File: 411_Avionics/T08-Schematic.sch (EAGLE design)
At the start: 34 parts, among them IC1 BQ24022, J1 USB-MICROB, U2 M25P10-AVMN6TP_TR, U3 LSM9DS0, U5 LTC1998, U6 ATMEGA32U4-AU, X1 8MHz

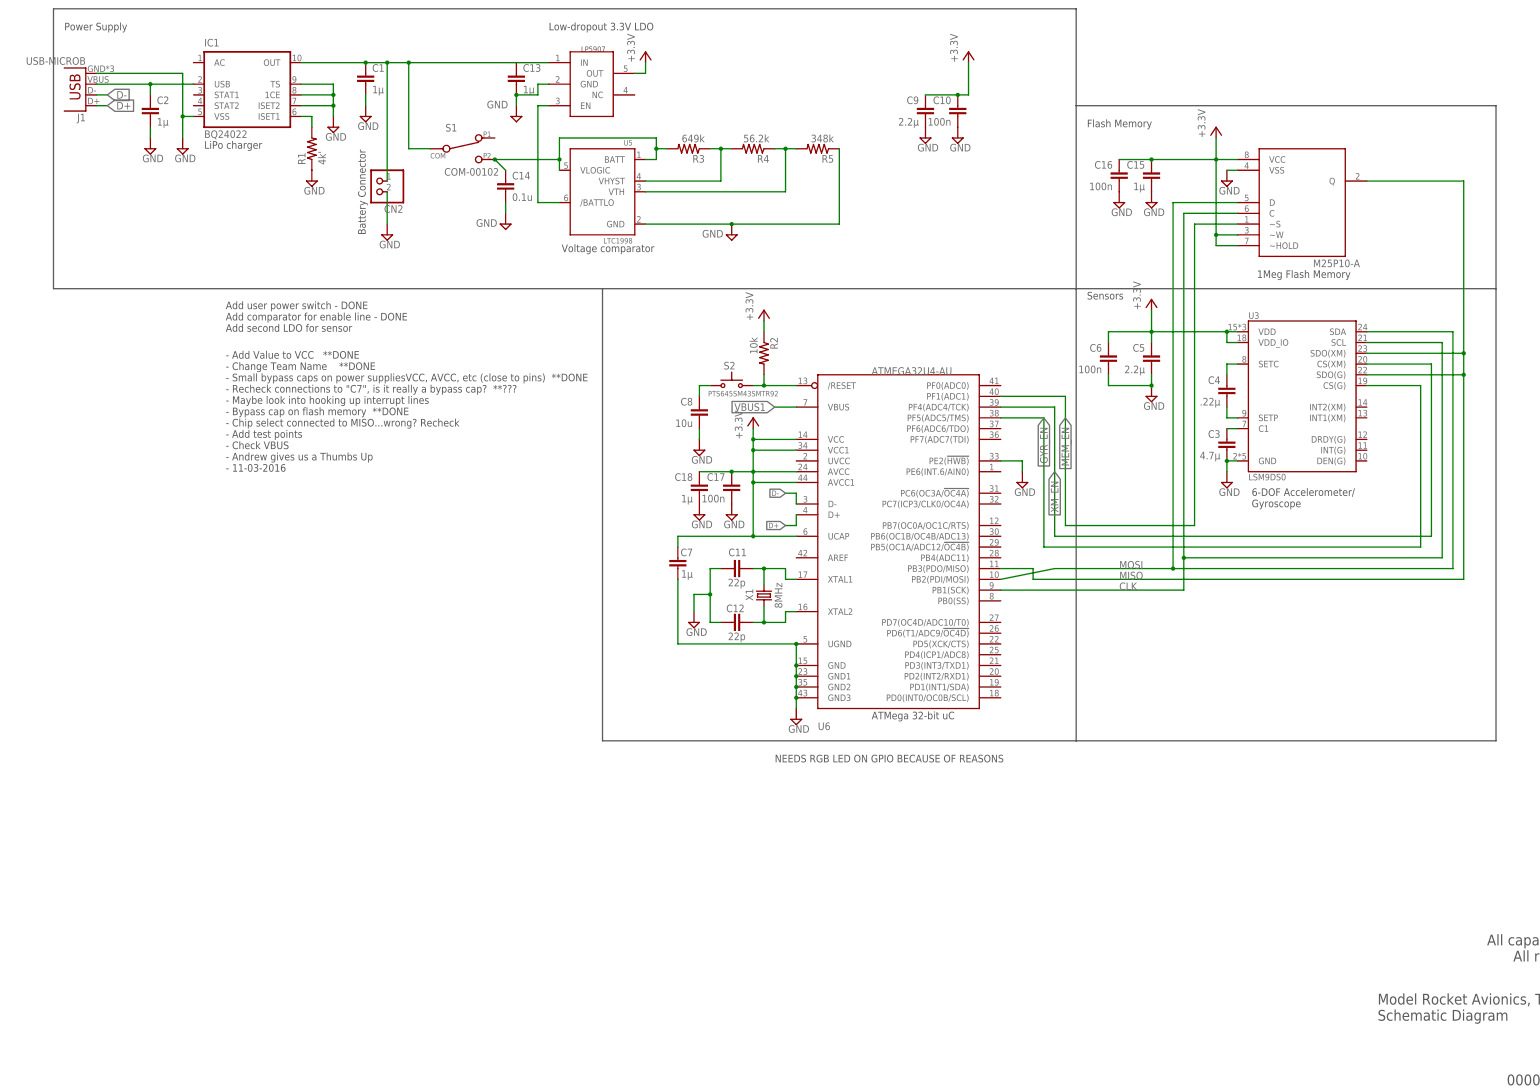
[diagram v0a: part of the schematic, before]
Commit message: Added RGB LED & resolved several ERC errors
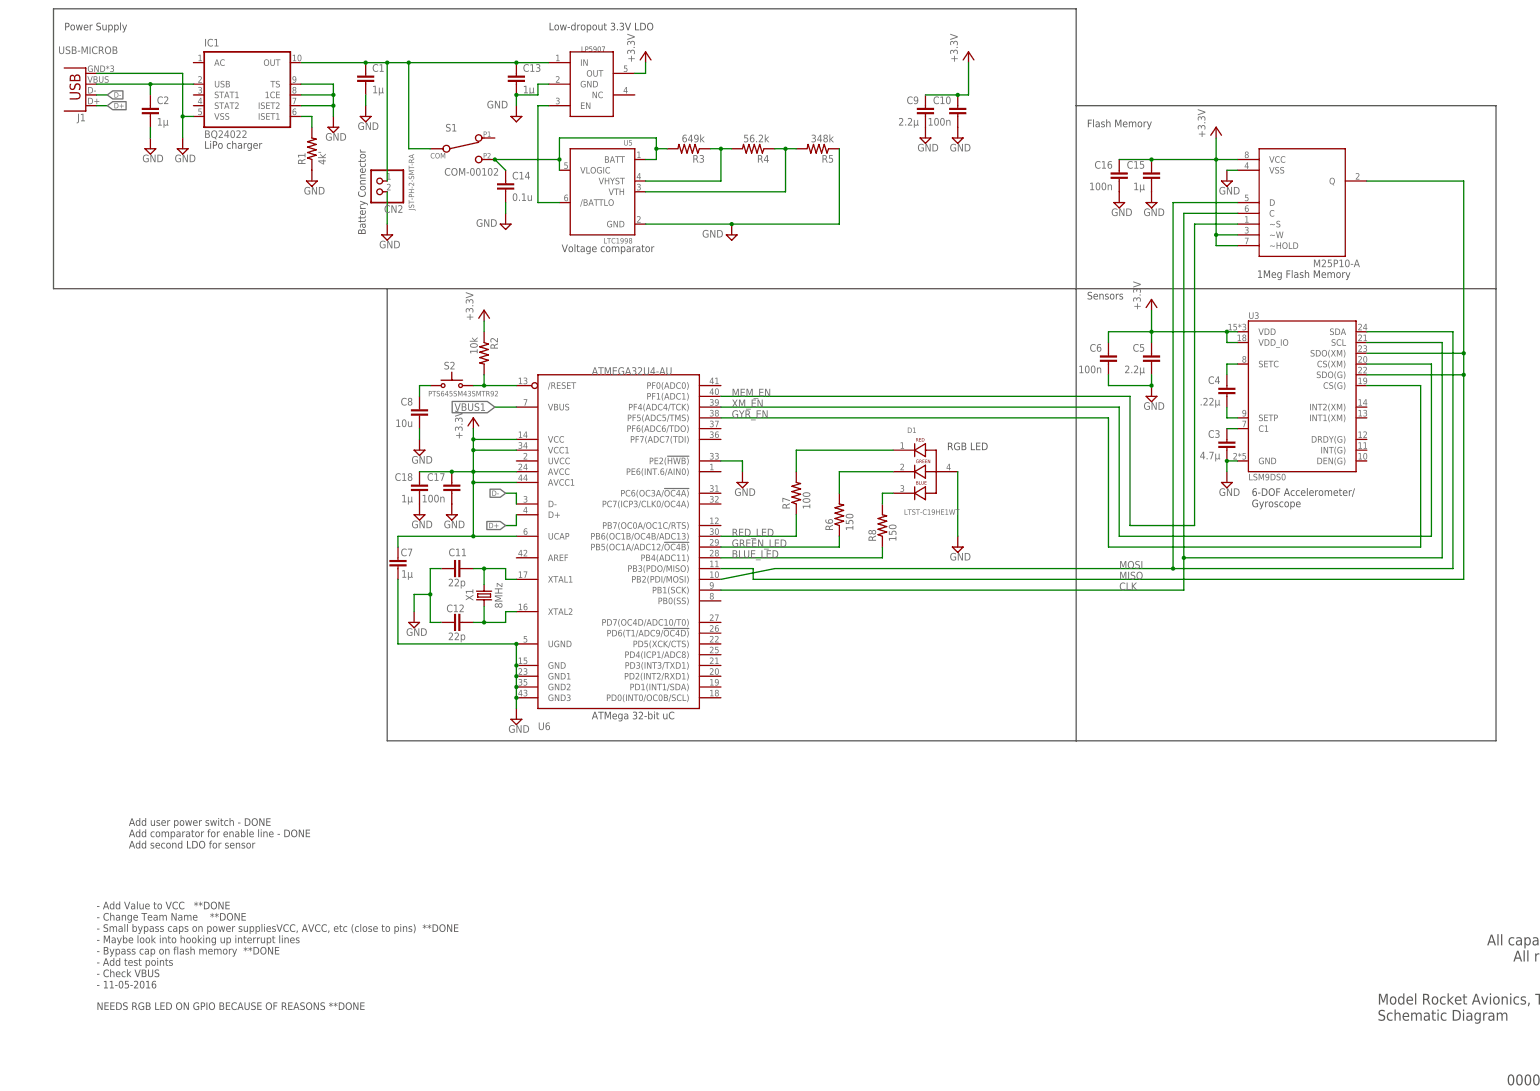
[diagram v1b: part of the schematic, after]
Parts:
- added D1: LTST-C19HE1WT, LTST-C19HE1WT:LTST-C19HE1WT
- added R6, R8: 150, rcl:R-US_R0805
- added R7: 100, rcl:R-US_R0805
- CN2: value (none) -> JST-PH-2-SMT-RA
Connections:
- new net BLUE_LED: R8.1, U6.PB4(ADC11)
- new net GREEN_LED: R6.1, U6.PB5(OC1A/ADC12/!OC4B)
- new net N$8: D1.3, R8.2
- new net RED_LED: R7.1, U6.PB6(OC1B/OC4B/ADC13)
- net GND: now also C13.2, D1.4, U$2.GND
- net N$1: now also D1.1, R7.2; no longer C2.1, IC1G$1.USB, J1.VBUS
- net N$13: now also C13.1
- net N$7: now also D1.2, R6.2; no longer C13.2, U$2.GND
- net VBUS1: now also C2.1, IC1G$1.USB, J1.VBUS
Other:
- note added: "- Add Value to VCC **DONE - Change Team Name **DONE - Small bypass caps on power suppliesVCC, AVCC, etc (close to pins) **DONE - Maybe look into hooking up interrupt lines - Bypass cap on flash memory **DONE - Add test points - Check VBUS - 11-05-2016"
- note added: "NEEDS RGB LED ON GPIO BECAUSE OF REASONS **DONE"
- note added: "RGB LED"
- note removed: "- Add Value to VCC **DONE - Change Team Name **DONE - Small bypass caps on power suppliesVCC, AVCC, etc (close to pins) **DONE - Recheck connections to "C7", is it really a bypass cap? **??? - Maybe look into hooking up interrupt lines - Bypass cap on flash memory **DONE - Chip select connected to MISO...wrong? Recheck - Add test points - Check VBUS - Andrew gives us a Thumbs Up - 11-03-2016"
- note removed: "NEEDS RGB LED ON GPIO BECAUSE OF REASONS"
- moved on the sheet: C11, C12, C17, C18, C7, C8, R2, S2, U6, X1
